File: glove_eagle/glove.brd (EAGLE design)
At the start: 63.5 x 38.1 mm, 20 parts, among them U1 BNO055, U2 NRF51822-QFAA-T

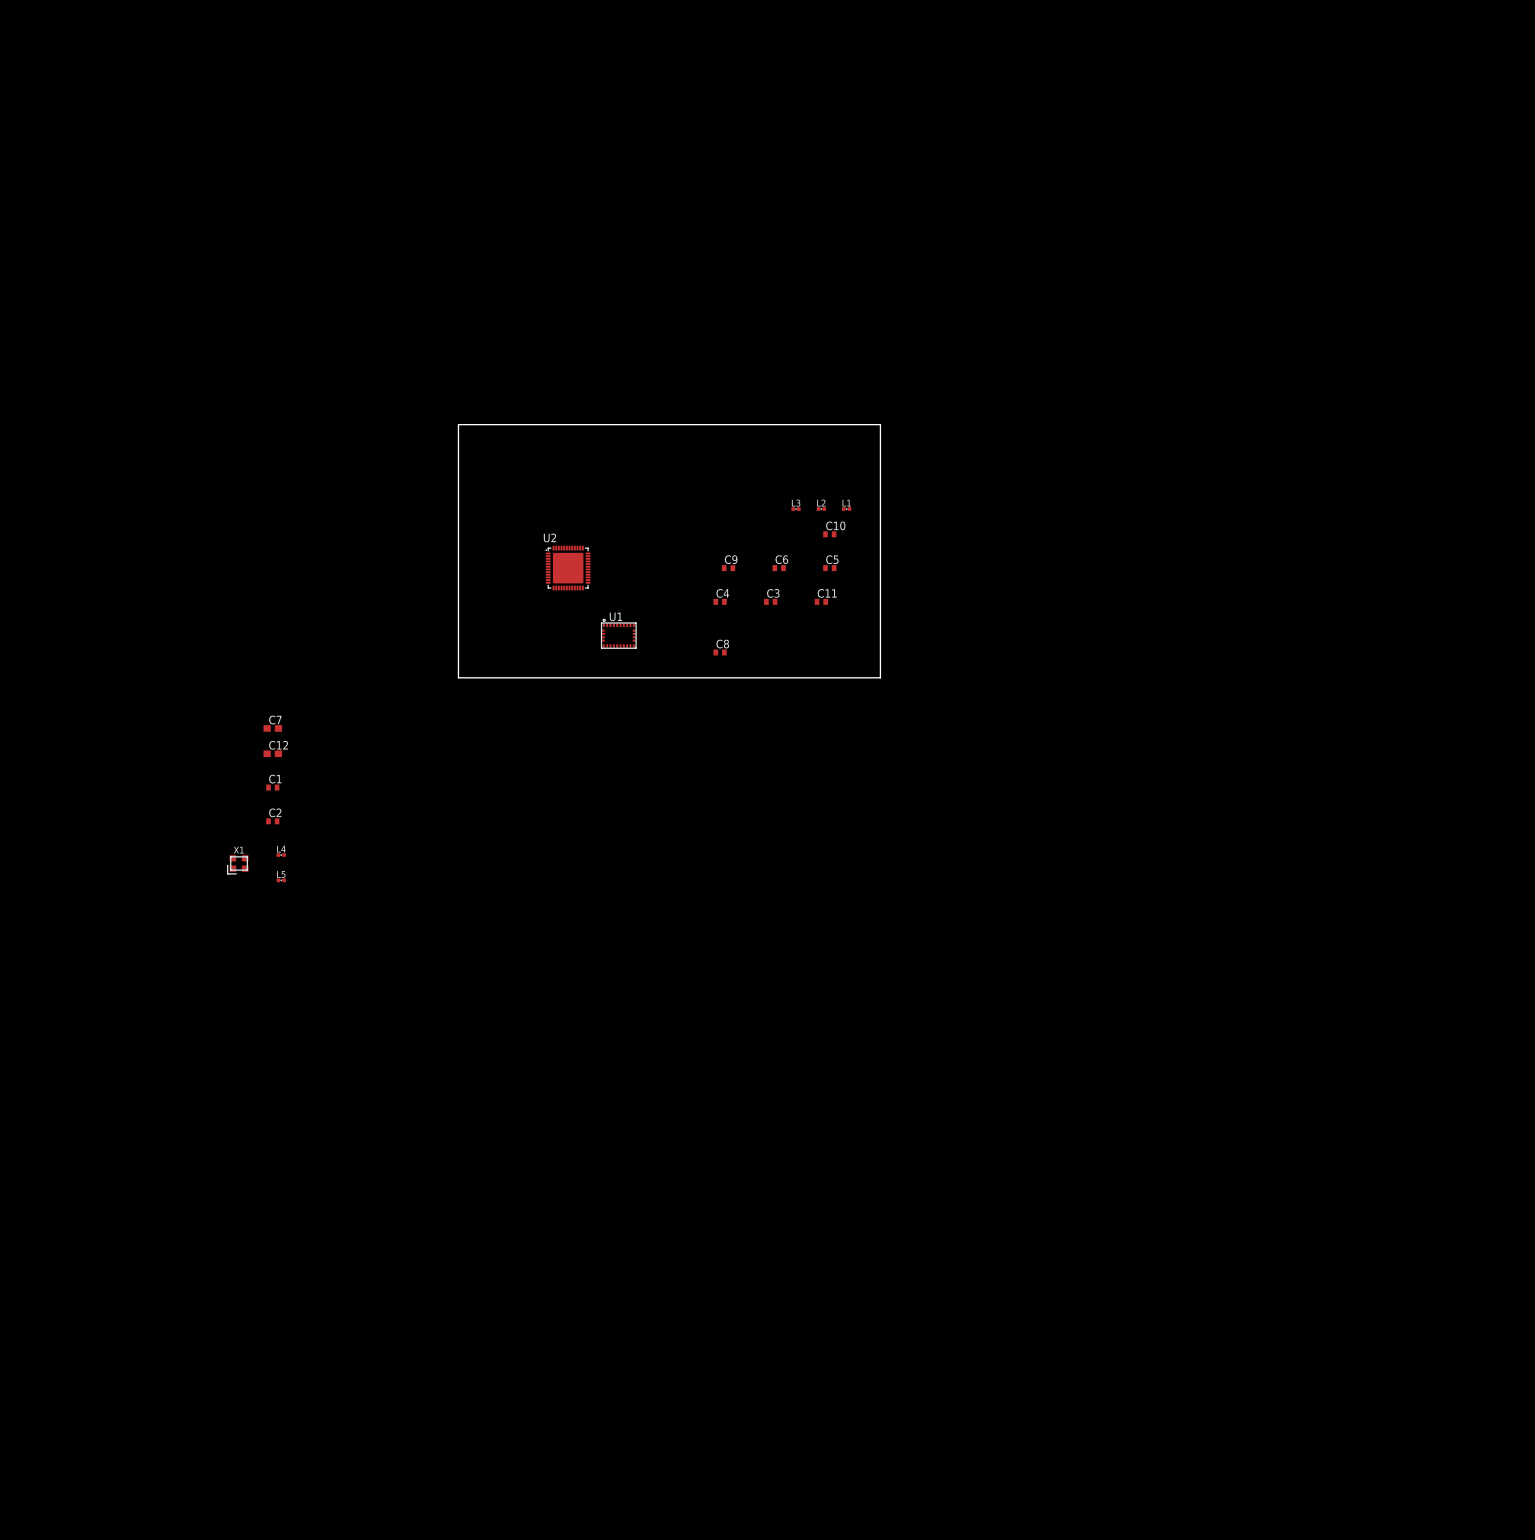
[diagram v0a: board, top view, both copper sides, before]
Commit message: Added Lab 11 libraries / Started charging circuit
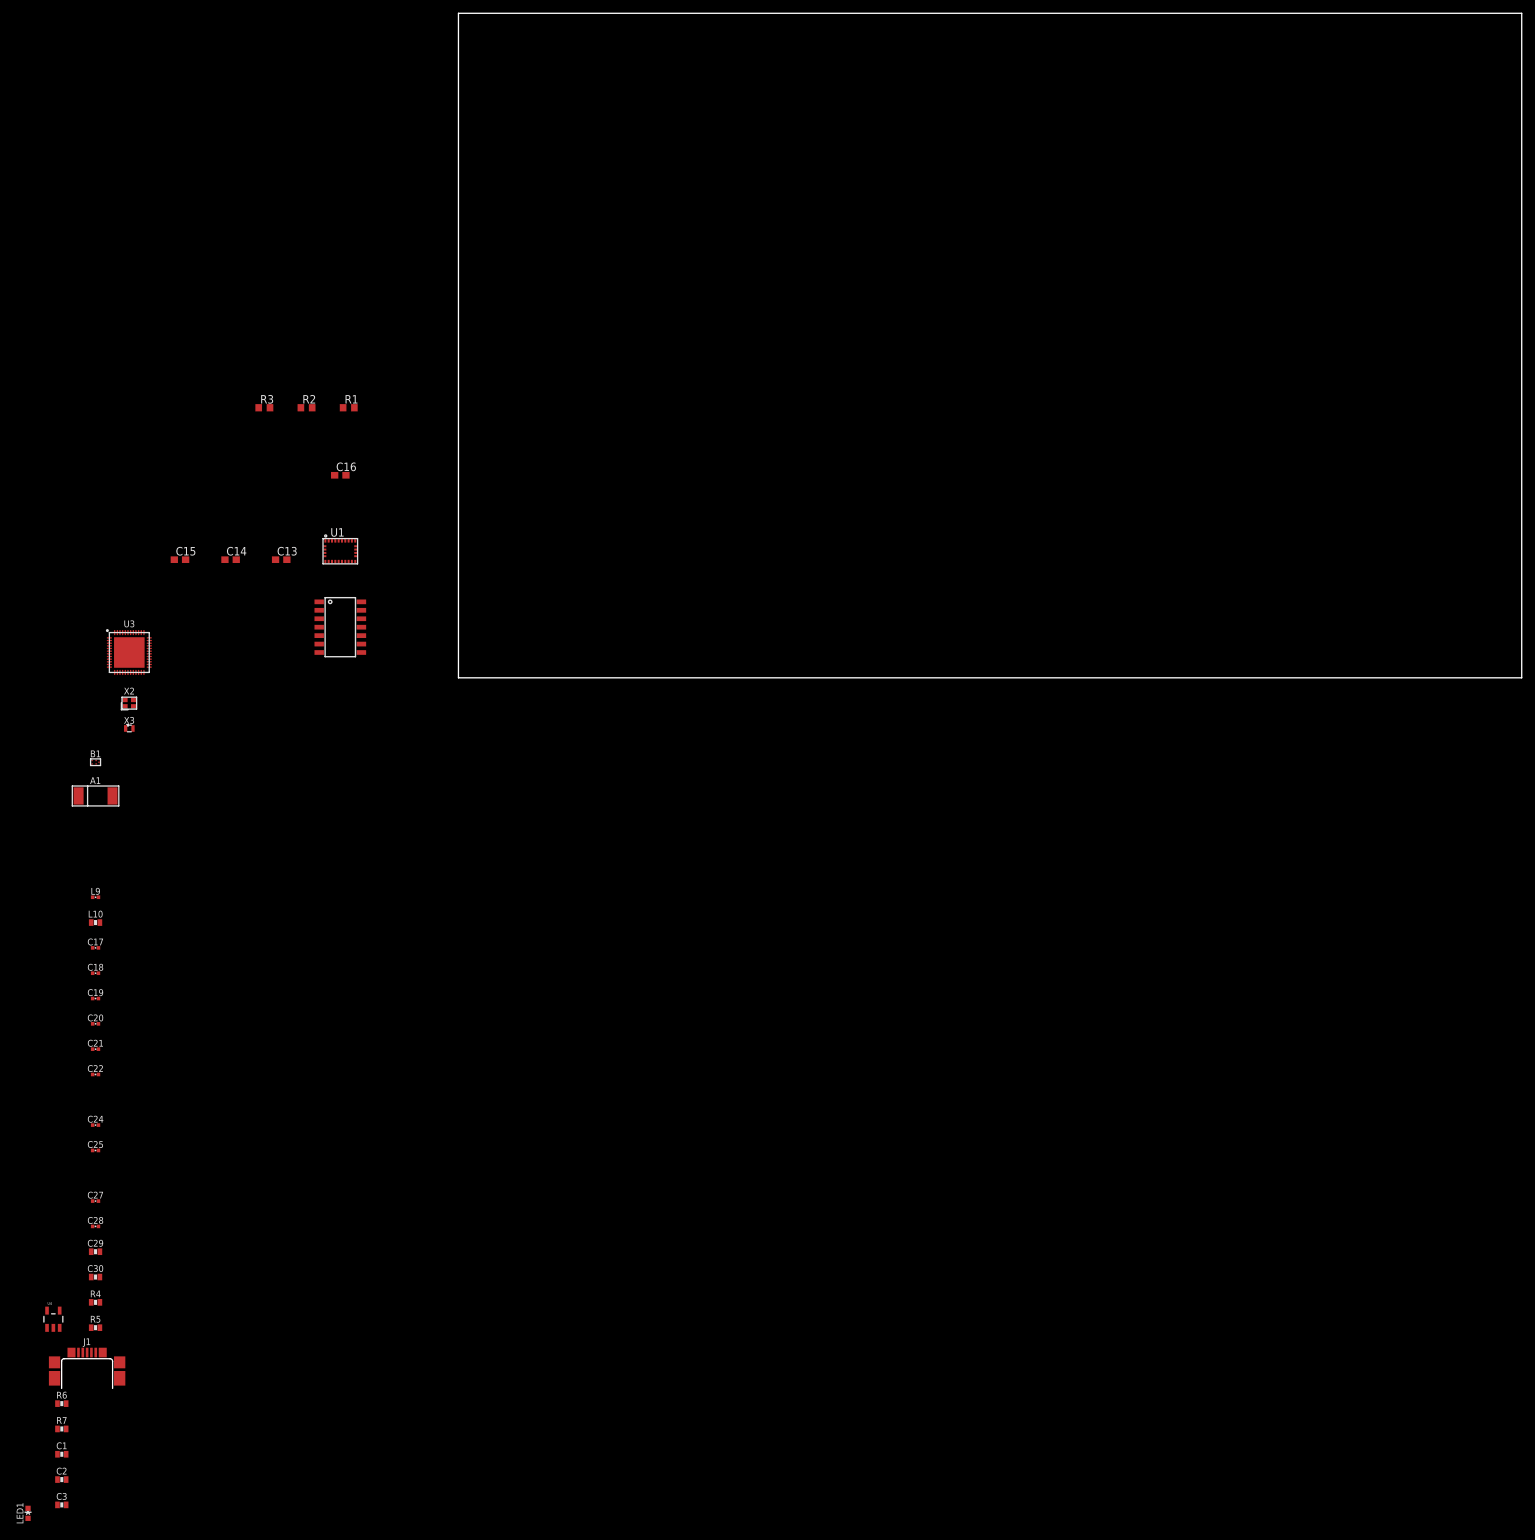
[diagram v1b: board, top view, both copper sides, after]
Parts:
- removed C10: 47 nF, rcl:C0402
- removed C11, C8: 100 nF, rcl:C0402
- removed C12: 1.0 uF, rcl:C0603
- removed C4: 1.0 pF, rcl:C0402
- removed C5: 3.9 pF, rcl:C0402
- removed C6: 1.5 pF, rcl:C0402
- removed C7: 4.7 uF, rcl:C0603
- removed C9: 1.0 nF, rcl:C0402
- removed L1: 4.7 nH, passives:0402_CAP
- removed L2, L4, L5: 27 nH, passives:0402_CAP
- removed L3: 3.3 nH, passives:0402_CAP
- removed U2: NRF51822-QFAA-T, NRF51822-QFAA-T:QFN40P600X600X90-49N
- removed X1: (no value), crystals:FHXXX
- added A1: FRACTUS-2.4GHZ-FR05-S1-N-0-102, chips:FRACTUS-ANTENNA-FR05-S1-N-0-102
- added B1: BAL-NRF01D3, chips:BAL-NRF01D3
- added C13, C14: 100 nF, rcl:C0603
- added C15: 120 nF, rcl:C0603
- added C16: 6.8 nF, rcl:C0603
- added C17, C18, C19, C20: 12 pF, passives:0402_CAP
- added C21: 2.2 nF, passives:0402_CAP
- added C22, C27: 1.0 nF, passives:0402_CAP
- added C24: 0.8 pF, passives:0402_CAP
- added C25: 100 nF, passives:0402_CAP
- added C28: 47 nF, passives:0402_CAP
- added C29: 4.7 uF, passives:0603_CAP
- added C30: 1.0 uF, passives:0603_CAP
- added J1: MICRO_USB_B_JST_MC5BR3-M404-4S, connector:USB_MICRO_B-JST-MC5BR3-M404-4S-TB
- added L10: 10 uH, passives:0603_CAP
- added L9: 15 nH, passives:0402_CAP
- added LED1: LED0603, leds:LED-0603
- added R1, R2, R3: 10 K, rcl:R0603
- added R4, R5, R6, R7: (no value), passives:0603-RES
- added U$1: QT1070, QT1070:QT1070
- added U3: NRF51822QF, chips:QFN-48-6MM
- added U4: MCP73831, SparkFun-PowerIC:SOT23-5
- added X2: (no value), crystals:TXC-8Y
- added X3: ABS05-32.768KHZ-9-T, crystals:ABS05
- C1, C2: value 12 pF -> (none); device rcl:C0402 -> passives:0603_CAP
- C3: value 2.2 nF -> (none); device rcl:C0402 -> passives:0603_CAP
- moved C3 172.8 mm to (-59.7, -124.5)
- moved C1 105.2 mm to (-59.7, -116.8)
- moved C2 104.0 mm to (-59.7, -120.7)
- moved U1 43.8 mm to (-17.8, 19.1)
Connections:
- removed net EXP: U2.49
- removed net N$10: L4.1, U2.2
- removed net N$11: L4.2, L5.2
- removed net N$13: C2.1, U2.37, X1.3
- removed net N$5: C5.1, L1.2, U2.32
- removed net N$6: C3.1, L2.1, U2.30
- removed net N$7: C4.1, C5.2, L3.1
- removed net N$8: C6.1, L3.2
- removed net PIN10: U1.10
- removed net PIN15: U1.15
- removed net PIN16: U1.16
- removed net XC2: C1.1, U2.38, X1.1
- new net GNDIO: C13.2, C14.2, C15.2, C16.2, U1.10, U1.15, U1.16, U1.18, U1.2, U1.25
- new net I2C_ADDR_SEL: U1.17
- new net INT: U1.14
- new net N$12: U1.5, U1.6
- new net N$14: L10.2, U3.2
- new net N$15: L10.1, L9.2
- new net N$16: C27.1, C30.1, L9.1, U3.35, U3.36
- new net N$17: R2.1, U1.20
- new net N$18: R3.1, U1.4
- new net N$19: R4.2, U3.23
- new net N$20: C20.1, U3.38, X2.3
- new net N$21: B1.ANT1, U3.31
- new net N$22: B1.ANT2, U3.32
- new net N$23: B1.VCC, C21.1, U3.30
- new net N$24: A1.1, B1.SE, C24.1
- new net N$25: C28.1, U3.29
- new net N$26: C22.1, U3.39
- new net N$27: C17.1, U3.45, X3.A
- new net N$28: C18.1, U3.46, X3.B
- new net N$29: C19.1, U3.37, X2.1
- new net N$30: R5.2, U3.24
- new net N$38: C1.1, J1.1, R6.2, U4.4
- new net SCL: R1.1, U1.19
- net GND: now also B1.GND, C17.2, C18.2, C19.2, C20.2, C21.2, C22.2, C24.2, C25.2, C27.2, C28.2, C29.2, C3.2, C30.2, J1.5, R4.1, R5.1, R7.1, U3.13, U3.33, U3.34, U3.GND, U4.2; no longer C4.2, C6.2, U1.2, U1.25, U2.13, U2.33, U2.34
- net N$1: now also C2.1, C3.1, U4.3; no longer C10.2, C11.2, C12.2, C3.2, C7.2, C8.2, C9.2
- net N$2: now also LED1.A, R6.1; no longer L1.1, L2.2, U2.31
- net N$3: now also LED1.C, U4.1; no longer C8.1, U2.39
- net N$4: now also R7.2, U4.5; no longer C10.1, U2.29
- net N$9: now also C13.1
- net VCC: now also C25.1, C29.1, U3.1, U3.12; no longer C11.1, C12.1, C7.1, C9.1, L5.1, U2.1, U2.12, U2.35, U2.36
- net VDD: now also C14.1, C15.1, C16.1, R1.2, R2.2, R3.2
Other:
- board size 63.5 x 38.1 mm -> 160 x 100 mm
